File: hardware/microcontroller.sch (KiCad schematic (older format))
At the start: 13 parts

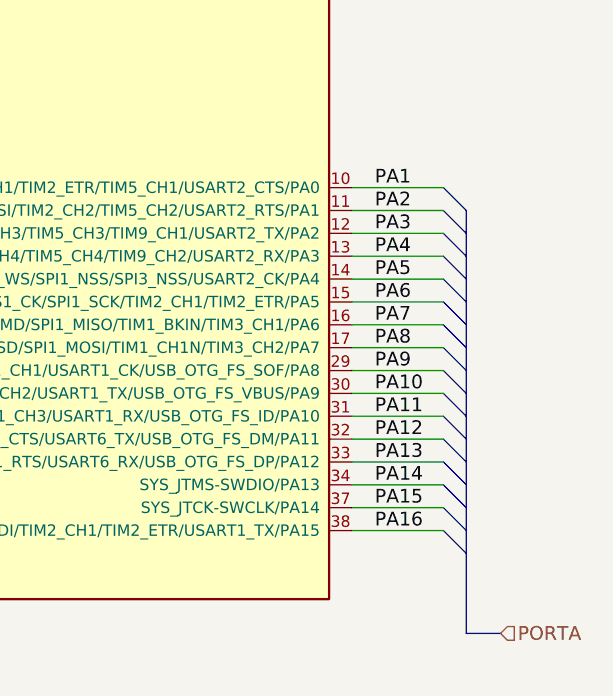
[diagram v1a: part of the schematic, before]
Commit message: Fix the PORT A numbering. Add the ST Link JTAG connector
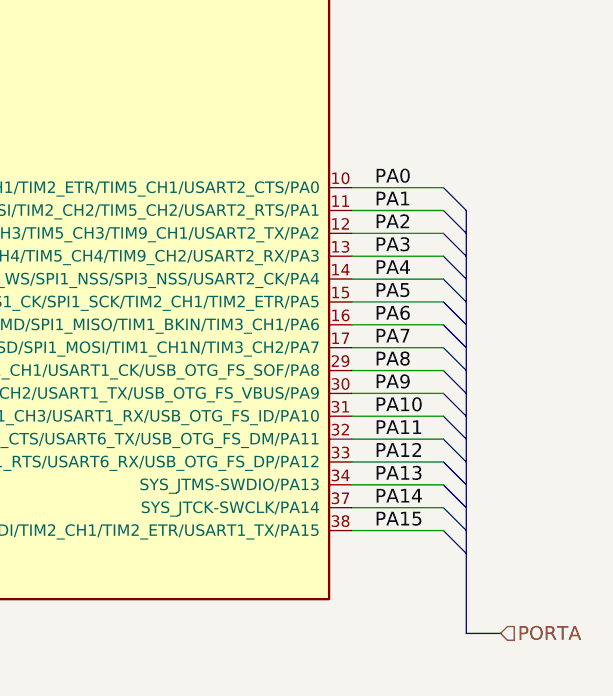
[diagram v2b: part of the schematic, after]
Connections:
- net labels added: PA0
- net labels removed: PA16
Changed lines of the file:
@@
 Wire Bus Line
 	1800 5250 1650 5250
-Text Label 9800 3300 0    60   ~ 0
-PA1
-Text Label 9800 3400 0    60   ~ 0
-PA2
-Text Label 9800 3500 0    60   ~ 0
-PA3
-Text Label 9800 3600 0    60   ~ 0
-PA4
-Text Label 9800 3700 0    60   ~ 0
-PA5
-Text Label 9800 3800 0    60   ~ 0
-PA6
-Text Label 9800 3900 0    60   ~ 0
-PA7
-Text Label 9800 4000 0    60   ~ 0
-PA8
-Text Label 9800 4100 0    60   ~ 0
-PA9
-Text Label 9800 4200 0    60   ~ 0
-PA10
-Text Label 9800 4300 0    60   ~ 0
-PA11
-Text Label 9800 4400 0    60   ~ 0
-PA12
-Text Label 9800 4500 0    60   ~ 0
-PA13
-Text Label 9800 4600 0    60   ~ 0
-PA14
-Text Label 9800 4700 0    60   ~ 0
-PA15
-Text Label 9800 4800 0    60   ~ 0
-PA16
 Wire Wire Line
 	9700 3300 10100 3300
@@
 Text Notes 1500 6350 0    60   ~ 0
 Boot Mode Select BOOT1
+Text Label 9800 3300 0    60   ~ 0
+PA0
+Text Label 9800 3400 0    60   ~ 0
+PA1
+Text Label 9800 3500 0    60   ~ 0
+PA2
+Text Label 9800 3600 0    60   ~ 0
+PA3
+Text Label 9800 3700 0    60   ~ 0
+PA4
+Text Label 9800 3800 0    60   ~ 0
+PA5
+Text Label 9800 3900 0    60   ~ 0
+PA6
+Text Label 9800 4000 0    60   ~ 0
+PA7
+Text Label 9800 4100 0    60   ~ 0
+PA8
+Text Label 9800 4200 0    60   ~ 0
+PA9
+Text Label 9800 4300 0    60   ~ 0
+PA10
+Text Label 9800 4400 0    60   ~ 0
+PA11
+Text Label 9800 4500 0    60   ~ 0
+PA12
+Text Label 9800 4600 0    60   ~ 0
+PA13
+Text Label 9800 4700 0    60   ~ 0
+PA14
+Text Label 9800 4800 0    60   ~ 0
+PA15
 $EndSCHEMATC

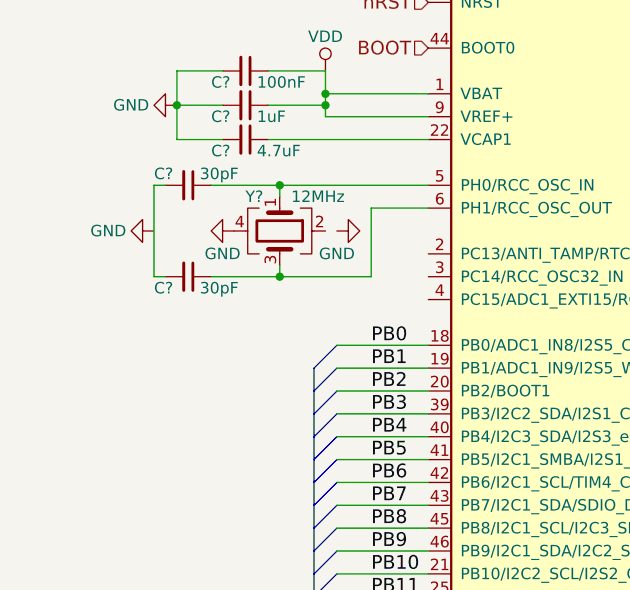
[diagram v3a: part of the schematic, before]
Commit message: Add the camera and finish off the schematic.
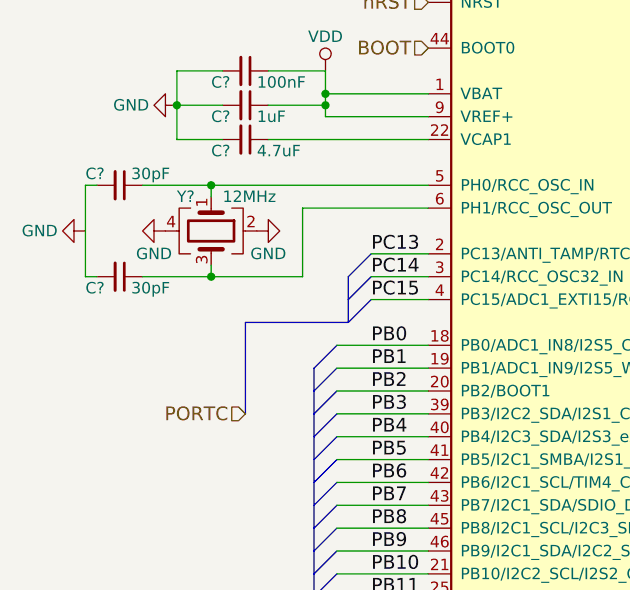
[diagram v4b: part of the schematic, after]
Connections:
- net labels added: PC13, PC14, PC15, PORTC
- wire segments 74 -> 77
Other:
- moved on the sheet: C?, Y?
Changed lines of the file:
@@
 L Crystal_GND24 Y?
 U 1 1 59427C05
-P 1650 2900
-F 0 "Y?" V 1500 2750 50  0000 L CNN
-F 1 "12MHz" V 1500 2950 50  0000 L CNN
-F 2 "" H 1650 2900 50  0001 C CNN
-F 3 "" H 1650 2900 50  0001 C CNN
-	1    1650 2900
+P 1350 2900
+F 0 "Y?" V 1200 2750 50  0000 L CNN
+F 1 "12MHz" V 1200 2950 50  0000 L CNN
+F 2 "" H 1350 2900 50  0001 C CNN
+F 3 "" H 1350 2900 50  0001 C CNN
+	1    1350 2900
 	0    1    1    0
 $EndComp
 Wire Wire Line
-	2300 2800 2050 2800
+	2300 2800 1750 2800
 Wire Wire Line
-	2050 2800 2050 3100
+	1750 2800 1750 3100
 Wire Wire Line
-	1100 3100 1100 2700
+	800  3100 800  2700
 Wire Wire Line
-	1650 2750 1650 2700
-Connection ~ 1650 2700
+	1350 2750 1350 2700
+Connection ~ 1350 2700
 Wire Wire Line
-	1650 3050 1650 3100
-Connection ~ 1650 3100
+	1350 3050 1350 3100
+Connection ~ 1350 3100
 $Comp
 L GND #PWR?
 U 1 1 59427C13
-P 1450 2900
-F 0 "#PWR?" H 1450 2650 50  0001 C CNN
-F 1 "GND" V 1550 2850 50  0000 C CNN
-F 2 "" H 1450 2900 50  0001 C CNN
-F 3 "" H 1450 2900 50  0001 C CNN
-	1    1450 2900
+P 1150 2900
+F 0 "#PWR?" H 1150 2650 50  0001 C CNN
+F 1 "GND" V 1250 2850 50  0000 C CNN
+F 2 "" H 1150 2900 50  0001 C CNN
+F 3 "" H 1150 2900 50  0001 C CNN
+	1    1150 2900
 	0    1    1    0
 $EndComp
@@
 L GND #PWR?
 U 1 1 59427C19
-P 1900 2900
-F 0 "#PWR?" H 1900 2650 50  0001 C CNN
-F 1 "GND" V 1800 2900 50  0000 C CNN
-F 2 "" H 1900 2900 50  0001 C CNN
-F 3 "" H 1900 2900 50  0001 C CNN
-	1    1900 2900
+P 1550 2900
+F 0 "#PWR?" H 1550 2650 50  0001 C CNN
+F 1 "GND" V 1450 2850 50  0000 C CNN
+F 2 "" H 1550 2900 50  0001 C CNN
+F 3 "" H 1550 2900 50  0001 C CNN
+	1    1550 2900
 	0    -1   -1   0
 $EndComp
@@
 L C_Small C?
 U 1 1 59427C1F
-P 1250 3100
-F 0 "C?" V 1300 2950 50  0000 L CNN
-F 1 "30pF" V 1300 3150 50  0000 L CNN
-F 2 "" H 1250 3100 50  0001 C CNN
-F 3 "" H 1250 3100 50  0001 C CNN
-	1    1250 3100
+P 950 3100
+F 0 "C?" V 1000 2950 50  0000 L CNN
+F 1 "30pF" V 1000 3150 50  0000 L CNN
+F 2 "" H 950 3100 50  0001 C CNN
+F 3 "" H 950 3100 50  0001 C CNN
+	1    950  3100
 	0    1    1    0
 $EndComp
 Wire Wire Line
-	1100 3100 1150 3100
+	800  3100 850  3100
 Wire Wire Line
-	2050 3100 1350 3100
+	1750 3100 1050 3100
 $Comp
 L C_Small C?
 U 1 1 59427C28
-P 1250 2700
-F 0 "C?" V 1200 2550 50  0000 L CNN
-F 1 "30pF" V 1200 2750 50  0000 L CNN
-F 2 "" H 1250 2700 50  0001 C CNN
-F 3 "" H 1250 2700 50  0001 C CNN
-	1    1250 2700
+P 950 2700
+F 0 "C?" V 900 2550 50  0000 L CNN
+F 1 "30pF" V 900 2750 50  0000 L CNN
+F 2 "" H 950 2700 50  0001 C CNN
+F 3 "" H 950 2700 50  0001 C CNN
+	1    950  2700
 	0    1    1    0
 $EndComp
 Wire Wire Line
-	1100 2700 1150 2700
+	800  2700 850  2700
 Wire Wire Line
-	1350 2700 2300 2700
+	1050 2700 2300 2700
 $Comp
 L GND #PWR?
 U 1 1 59427C31
-P 1100 2900
-F 0 "#PWR?" H 1100 2650 50  0001 C CNN
-F 1 "GND" V 1100 2700 50  0000 C CNN
-F 2 "" H 1100 2900 50  0001 C CNN
-F 3 "" H 1100 2900 50  0001 C CNN
-	1    1100 2900
+P 800 2900
+F 0 "#PWR?" H 800 2650 50  0001 C CNN
+F 1 "GND" V 800 2700 50  0000 C CNN
+F 2 "" H 800 2900 50  0001 C CNN
+F 3 "" H 800 2900 50  0001 C CNN
+	1    800  2900
 	0    1    1    0
 $EndComp
@@
 Text Label 9800 4800 0    60   ~ 0
 PA15
+Text Label 2050 3000 0    60   ~ 0
+PC13
+Text Label 2050 3100 0    60   ~ 0
+PC14
+Text Label 2050 3200 0    60   ~ 0
+PC15
+Wire Wire Line
+	2300 3000 2050 3000
+Wire Wire Line
+	2300 3100 2050 3100
+Wire Wire Line
+	2300 3200 2050 3200
+Entry Bus Bus
+	1950 3100 2050 3000
+Entry Bus Bus
+	1950 3200 2050 3100
+Entry Bus Bus
+	1950 3300 2050 3200
+Wire Bus Line
+	1950 3100 1950 3300
+Wire Bus Line
+	1950 3300 1500 3300
+Wire Bus Line
+	1500 3300 1500 3700
+Text HLabel 1500 3700 0    60   Input ~ 0
+PORTC
 $EndSCHEMATC

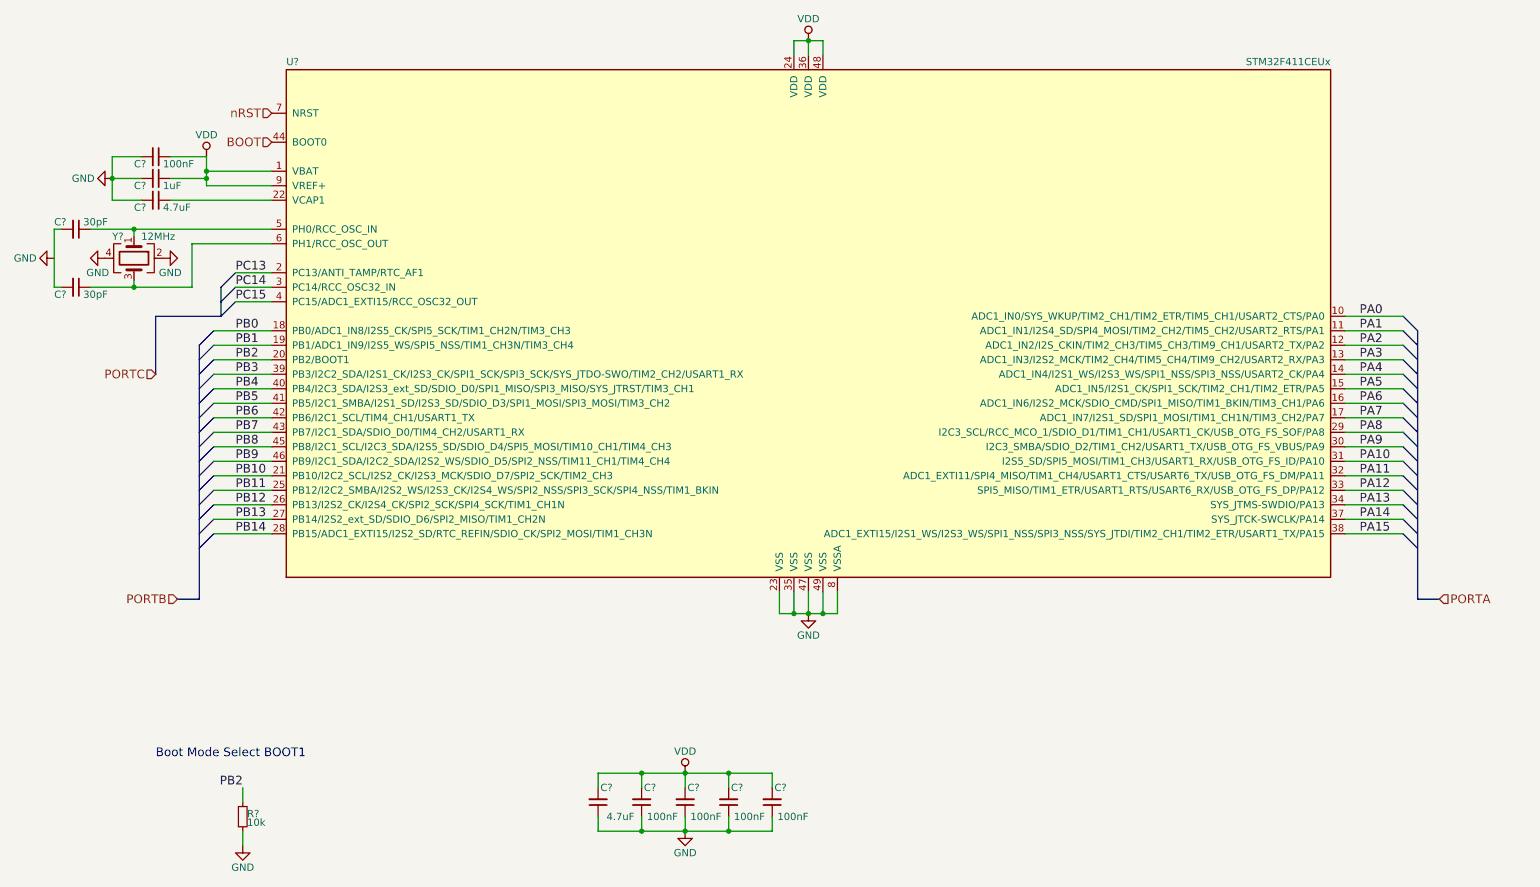
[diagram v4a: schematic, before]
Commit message: Add missing camera decoupling. Annotate all parts.
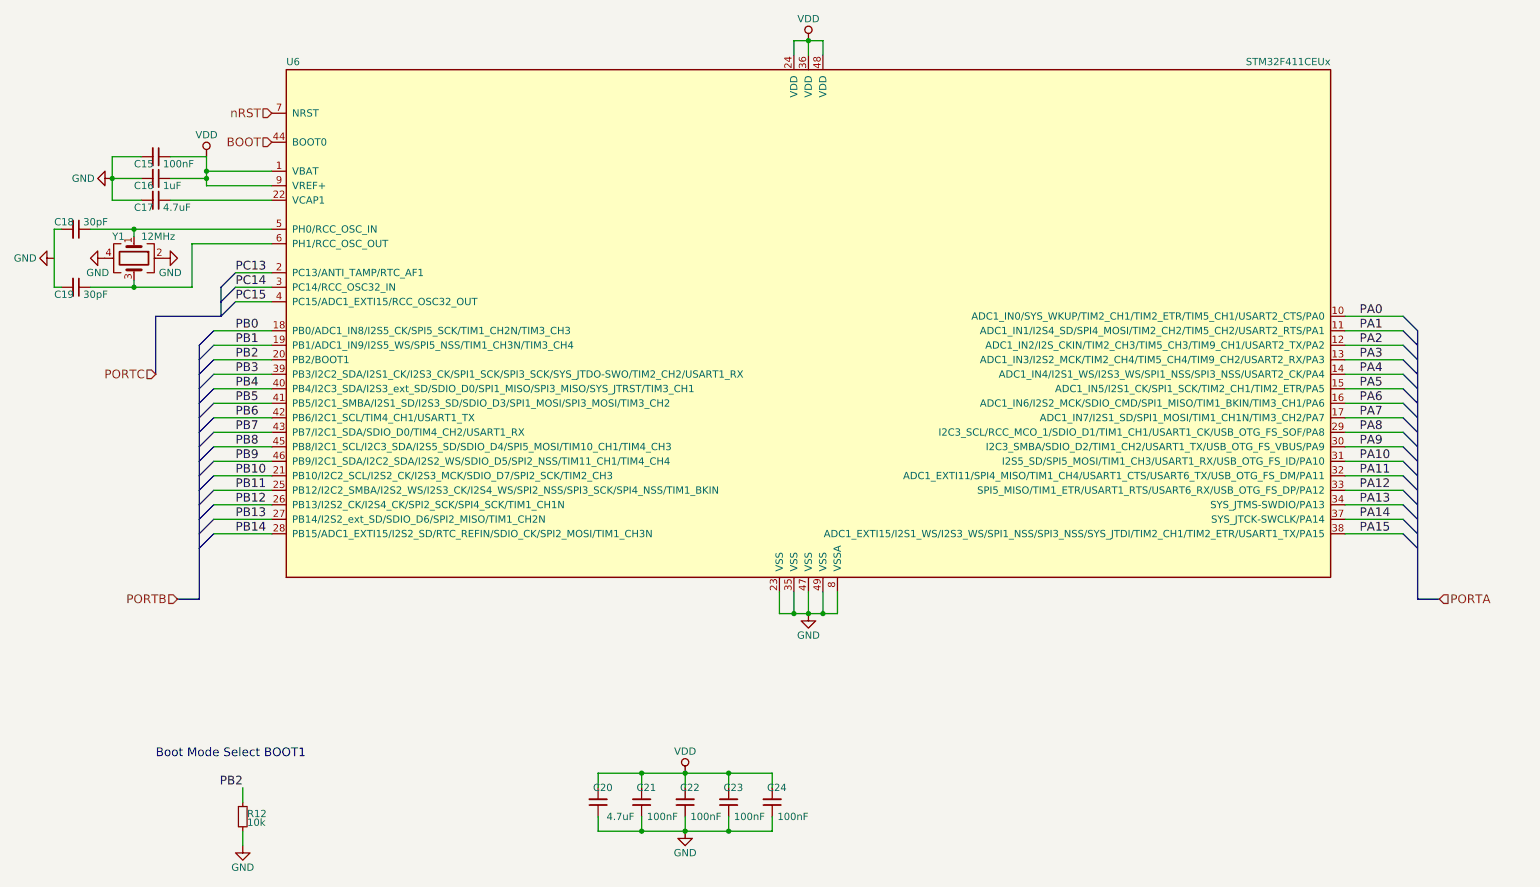
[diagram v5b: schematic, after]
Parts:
- gave numbers to parts that had none: 13
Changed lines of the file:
@@
 P 6000 3400
 AR Path="/59427B10" Ref="U?"  Part="1"
-AR Path="/59425D39/59427B10" Ref="U?"  Part="1"
-F 0 "U?" H 2400 5225 50  0000 L BNN
+AR Path="/59425D39/59427B10" Ref="U6"  Part="1"
+F 0 "U6" H 2400 5225 50  0000 L BNN
 F 1 "STM32F411CEUx" H 9600 5225 50  0000 R BNN
 F 2 "UFQFPN48" H 9600 5175 50  0001 R TNN
@@
 $EndComp
 $Comp
-L VDD #PWR?
+L VDD #PWR51
 U 1 1 59427B17
 P 6000 1400
-F 0 "#PWR?" H 6000 1250 50  0001 C CNN
+F 0 "#PWR51" H 6000 1250 50  0001 C CNN
 F 1 "VDD" H 6000 1550 50  0000 C CNN
 F 2 "" H 6000 1400 50  0001 C CNN
@@
 $EndComp
 $Comp
-L VDD #PWR?
+L VDD #PWR52
 U 1 1 59427B1D
 P 1850 2200
-F 0 "#PWR?" H 1850 2050 50  0001 C CNN
+F 0 "#PWR52" H 1850 2050 50  0001 C CNN
 F 1 "VDD" H 1850 2350 50  0000 C CNN
 F 2 "" H 1850 2200 50  0001 C CNN
@@
 $EndComp
 $Comp
-L C_Small C?
+L C_Small C17
 U 1 1 59427B23
 P 1500 2500
-F 0 "C?" V 1550 2350 50  0000 L CNN
+F 0 "C17" V 1550 2350 50  0000 L CNN
 F 1 "4.7uF" V 1550 2550 50  0000 L CNN
 F 2 "" H 1500 2500 50  0001 C CNN
@@
 $EndComp
 $Comp
-L GND #PWR?
+L GND #PWR53
 U 1 1 59427B2A
 P 1200 2350
-F 0 "#PWR?" H 1200 2100 50  0001 C CNN
+F 0 "#PWR53" H 1200 2100 50  0001 C CNN
 F 1 "GND" V 1200 2150 50  0000 C CNN
 F 2 "" H 1200 2350 50  0001 C CNN
@@
 $EndComp
 $Comp
-L GND #PWR?
+L GND #PWR57
 U 1 1 59427B30
 P 6000 5350
-F 0 "#PWR?" H 6000 5100 50  0001 C CNN
+F 0 "#PWR57" H 6000 5100 50  0001 C CNN
 F 1 "GND" H 6000 5200 50  0000 C CNN
 F 2 "" H 6000 5350 50  0001 C CNN
@@
 $EndComp
 $Comp
-L C_Small C?
+L C_Small C16
 U 1 1 59427B36
 P 1500 2350
-F 0 "C?" V 1550 2200 50  0000 L CNN
+F 0 "C16" V 1550 2200 50  0000 L CNN
 F 1 "1uF" V 1550 2400 50  0000 L CNN
 F 2 "" H 1500 2350 50  0001 C CNN
@@
 $EndComp
 $Comp
-L C_Small C?
+L C_Small C15
 U 1 1 59427B3D
 P 1500 2200
-F 0 "C?" V 1550 2050 50  0000 L CNN
+F 0 "C15" V 1550 2050 50  0000 L CNN
 F 1 "100nF" V 1550 2250 50  0000 L CNN
 F 2 "" H 1500 2200 50  0001 C CNN
@@
 $EndComp
 $Comp
-L C_Small C?
+L C_Small C21
 U 1 1 59427B44
 P 4850 6650
-F 0 "C?" H 4750 6550 50  0000 L CNN
+F 0 "C21" H 4750 6550 50  0000 L CNN
 F 1 "100nF" H 4600 6750 50  0000 L CNN
 F 2 "" H 4850 6650 50  0001 C CNN
@@
 $EndComp
 $Comp
-L C_Small C?
+L C_Small C22
 U 1 1 59427B4B
 P 5150 6650
-F 0 "C?" H 5050 6550 50  0000 L CNN
+F 0 "C22" H 5050 6550 50  0000 L CNN
 F 1 "100nF" H 4900 6750 50  0000 L CNN
 F 2 "" H 5150 6650 50  0001 C CNN
@@
 $EndComp
 $Comp
-L C_Small C?
+L C_Small C23
 U 1 1 59427B52
 P 5450 6650
-F 0 "C?" H 5350 6550 50  0000 L CNN
+F 0 "C23" H 5350 6550 50  0000 L CNN
 F 1 "100nF" H 5200 6750 50  0000 L CNN
 F 2 "" H 5450 6650 50  0001 C CNN
@@
 $EndComp
 $Comp
-L C_Small C?
+L C_Small C24
 U 1 1 59427B59
 P 5750 6650
-F 0 "C?" H 5650 6550 50  0000 L CNN
+F 0 "C24" H 5650 6550 50  0000 L CNN
 F 1 "100nF" H 5500 6750 50  0000 L CNN
 F 2 "" H 5750 6650 50  0001 C CNN
@@
 $EndComp
 $Comp
-L GND #PWR?
+L GND #PWR59
 U 1 1 59427B60
 P 5150 6850
-F 0 "#PWR?" H 5150 6600 50  0001 C CNN
+F 0 "#PWR59" H 5150 6600 50  0001 C CNN
 F 1 "GND" H 5150 6700 50  0000 C CNN
 F 2 "" H 5150 6850 50  0001 C CNN
@@
 $EndComp
 $Comp
-L VDD #PWR?
+L VDD #PWR58
 U 1 1 59427B66
 P 5150 6450
-F 0 "#PWR?" H 5150 6300 50  0001 C CNN
+F 0 "#PWR58" H 5150 6300 50  0001 C CNN
 F 1 "VDD" H 5150 6600 50  0000 C CNN
 F 2 "" H 5150 6450 50  0001 C CNN
@@
 $EndComp
 $Comp
-L C_Small C?
+L C_Small C20
 U 1 1 59427B6C
 P 4550 6650
-F 0 "C?" H 4450 6550 50  0000 L CNN
+F 0 "C20" H 4450 6550 50  0000 L CNN
 F 1 "4.7uF" H 4300 6750 50  0000 L CNN
 F 2 "" H 4550 6650 50  0001 C CNN
@@
 	10200 5250 10350 5250
 $Comp
-L Crystal_GND24 Y?
+L Crystal_GND24 Y1
 U 1 1 59427C05
 P 1350 2900
-F 0 "Y?" V 1200 2750 50  0000 L CNN
+F 0 "Y1" V 1200 2750 50  0000 L CNN
 F 1 "12MHz" V 1200 2950 50  0000 L CNN
 F 2 "" H 1350 2900 50  0001 C CNN
@@
 Connection ~ 1350 3100
 $Comp
-L GND #PWR?
+L GND #PWR55
 U 1 1 59427C13
 P 1150 2900
-F 0 "#PWR?" H 1150 2650 50  0001 C CNN
+F 0 "#PWR55" H 1150 2650 50  0001 C CNN
 F 1 "GND" V 1250 2850 50  0000 C CNN
 F 2 "" H 1150 2900 50  0001 C CNN
@@
 $EndComp
 $Comp
-L GND #PWR?
+L GND #PWR56
 U 1 1 59427C19
 P 1550 2900
-F 0 "#PWR?" H 1550 2650 50  0001 C CNN
+F 0 "#PWR56" H 1550 2650 50  0001 C CNN
 F 1 "GND" V 1450 2850 50  0000 C CNN
 F 2 "" H 1550 2900 50  0001 C CNN
@@
 $EndComp
 $Comp
-L C_Small C?
+L C_Small C19
 U 1 1 59427C1F
 P 950 3100
-F 0 "C?" V 1000 2950 50  0000 L CNN
+F 0 "C19" V 1000 2950 50  0000 L CNN
 F 1 "30pF" V 1000 3150 50  0000 L CNN
 F 2 "" H 950 3100 50  0001 C CNN
@@
 	1750 3100 1050 3100
 $Comp
-L C_Small C?
+L C_Small C18
 U 1 1 59427C28
 P 950 2700
-F 0 "C?" V 900 2550 50  0000 L CNN
+F 0 "C18" V 900 2550 50  0000 L CNN
 F 1 "30pF" V 900 2750 50  0000 L CNN
 F 2 "" H 950 2700 50  0001 C CNN
@@
 	1050 2700 2300 2700
 $Comp
-L GND #PWR?
+L GND #PWR54
 U 1 1 59427C31
 P 800 2900
-F 0 "#PWR?" H 800 2650 50  0001 C CNN
+F 0 "#PWR54" H 800 2650 50  0001 C CNN
 F 1 "GND" V 800 2700 50  0000 C CNN
 F 2 "" H 800 2900 50  0001 C CNN
@@
 PB2
 $Comp
-L R_Small R?
+L R_Small R12
 U 1 1 594293DA
 P 2100 6750
-F 0 "R?" H 2130 6770 50  0000 L CNN
+F 0 "R12" H 2130 6770 50  0000 L CNN
 F 1 "10k" H 2130 6710 50  0000 L CNN
 F 2 "" H 2100 6750 50  0001 C CNN
@@
 $EndComp
 $Comp
-L GND #PWR?
+L GND #PWR60
 U 1 1 5942944C
 P 2100 6950
-F 0 "#PWR?" H 2100 6700 50  0001 C CNN
+F 0 "#PWR60" H 2100 6700 50  0001 C CNN
 F 1 "GND" H 2100 6800 50  0000 C CNN
 F 2 "" H 2100 6950 50  0001 C CNN
